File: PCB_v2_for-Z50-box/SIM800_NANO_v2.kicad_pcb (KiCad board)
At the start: 2 copper layers, 108.8 x 83.1 mm, 42 parts, among them J1 PJ-002BH, J2 TB002-500-02BE, J3 Screw_Terminal_1x3, J4 Screw_Terminal_1x3, K1 SANYOU_SRD_Form_C, K2 SANYOU_SRD_Form_C, Q1 MMBT5551L, Q2 MMBT5551L, SW1 SIM800_RST, U1 LM2596S-ADJ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

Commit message: Modified vias
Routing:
- net GND: track 273.6 -> 256.5 mm, vias 7 -> 3
- net Net-(R8-Pad2): vias 1 -> 0
- net Net-(R7-Pad1): vias 1 -> 0
- net Net-(R2-Pad1): vias 1 -> 0
- net Net-(R12-Pad2): vias 1 -> 0
- net Net-(R11-Pad1): vias 1 -> 0
- net Net-(BR1-Pad2): vias 2 -> 1
- net Mains_sence: vias 1 -> 0
- net +5V: vias 3 -> 1

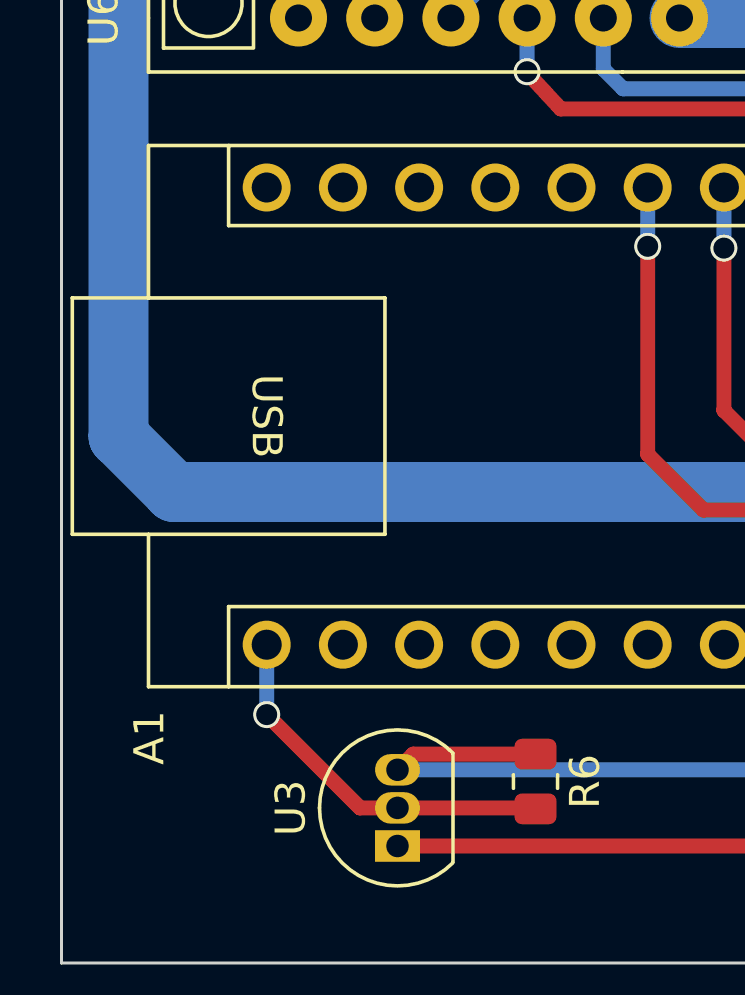
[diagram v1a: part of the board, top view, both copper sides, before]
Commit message: Temp sensor pin13 to pin12
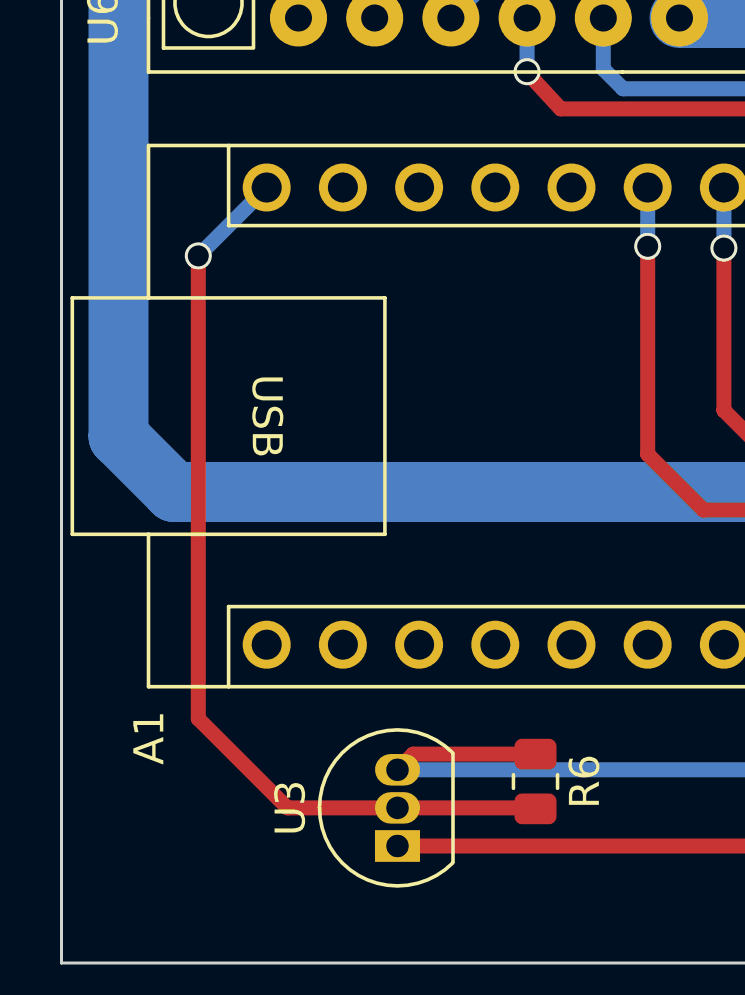
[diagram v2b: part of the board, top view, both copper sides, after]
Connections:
- A1 pad 15: unconnected-(A1-Pad15) -> Temp
- A1 pad 16: Temp -> unconnected-(A1-Pad16)
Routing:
- net Temp: track 12.6 -> 31.1 mm
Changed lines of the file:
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@@
   (net 8 "unconnected-(A1-Pad13)")
   (net 9 "unconnected-(A1-Pad14)")
-  (net 10 "unconnected-(A1-Pad15)")
+  (net 10 "unconnected-(A1-Pad16)")
   (net 11 "Temp")
   (net 12 "unconnected-(A1-Pad17)")
@@
       (net 9 "unconnected-(A1-Pad14)") (pinfunction "D11") (pintype "bidirectional+no_connect"))
     (pad "15" thru_hole oval (at 0 35.56 270) (size 1.6 1.6) (drill 1) (layers *.Cu *.Mask)
-      (net 10 "unconnected-(A1-Pad15)") (pinfunction "D12") (pintype "bidirectional+no_connect"))
+      (net 11 "Temp") (pinfunction "D12") (pintype "bidirectional"))
     (pad "16" thru_hole oval (at 15.24 35.56 270) (size 1.6 1.6) (drill 1) (layers *.Cu *.Mask)
-      (net 11 "Temp") (pinfunction "D13") (pintype "bidirectional"))
+      (net 10 "unconnected-(A1-Pad16)") (pinfunction "D13") (pintype "bidirectional+no_connect"))
     (pad "17" thru_hole oval (at 15.24 33.02 270) (size 1.6 1.6) (drill 1) (layers *.Cu *.Mask)
       (net 12 "unconnected-(A1-Pad17)") (pinfunction "3V3") (pintype "power_out+no_connect"))
@@
   (segment (start 107.14 119.96) (end 107.14 118) (width 0.5) (layer "B.Cu") (net 5))
   (segment (start 103.3675 138.68) (end 103.4 138.7125) (width 0.5) (layer "F.Cu") (net 11))
+  (segment (start 98.8 138.68) (end 95.132636 138.68) (width 0.5) (layer "F.Cu") (net 11))
   (segment (start 98.8 138.68) (end 103.3675 138.68) (width 0.5) (layer "F.Cu") (net 11))
-  (segment (start 94.44 135.57) (end 97.55 138.68) (width 0.5) (layer "F.Cu") (net 11))
-  (segment (start 97.55 138.68) (end 98.8 138.68) (width 0.5) (layer "F.Cu") (net 11))
-  (via (at 94.44 135.57) (size 0.9) (drill 0.7) (layers "F.Cu" "B.Cu") (net 11))
-  (segment (start 94.44 133.24) (end 94.44 135.57) (width 0.5) (layer "B.Cu") (net 11))
+  (segment (start 95.132636 138.68) (end 92.16 135.707364) (width 0.5) (layer "F.Cu") (net 11))
+  (segment (start 92.16 135.707364) (end 92.16 120.28) (width 0.5) (layer "F.Cu") (net 11))
+  (via (at 92.16 120.28) (size 0.9) (drill 0.7) (layers "F.Cu" "B.Cu") (net 11))
+  (segment (start 94.44 118) (end 92.16 120.28) (width 0.5) (layer "B.Cu") (net 11))
   (segment (start 156.095 94.505) (end 156.095 92.865) (width 0.5) (layer "F.Cu") (net 22))
   (segment (start 142.31 65.6) (end 139.9 65.6) (width 1) (layer "F.Cu") (net 22))
